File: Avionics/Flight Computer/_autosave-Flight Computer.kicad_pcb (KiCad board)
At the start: 2 copper layers, 50.8 x 50.8 mm, 28 parts, among them J1 CONN_COAXIAL, J2 CONN_COAXIAL, U1 CC1310F128RGZR, U2 CC1190RGVR, U3 CC2650F128RGZR, U4 CC2592RGVR

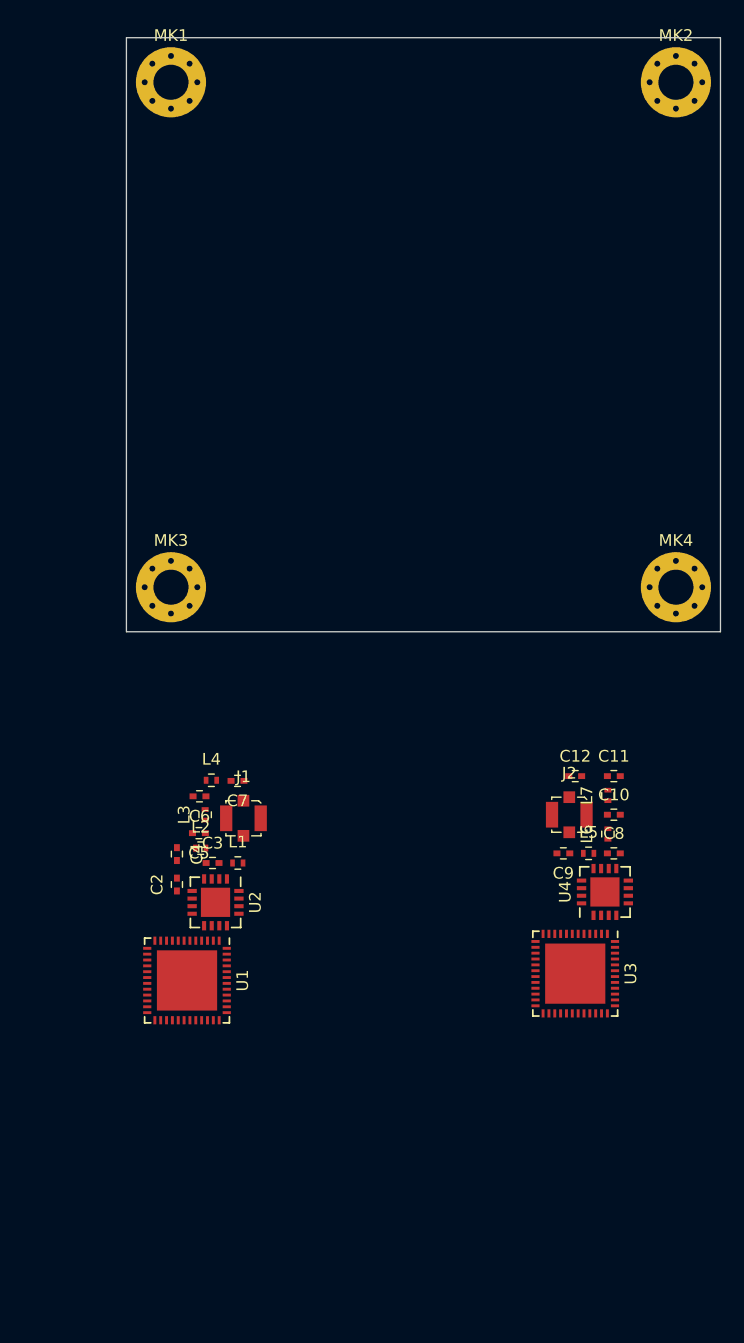
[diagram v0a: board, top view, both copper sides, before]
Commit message: Added framework and started capturing radio schematics.
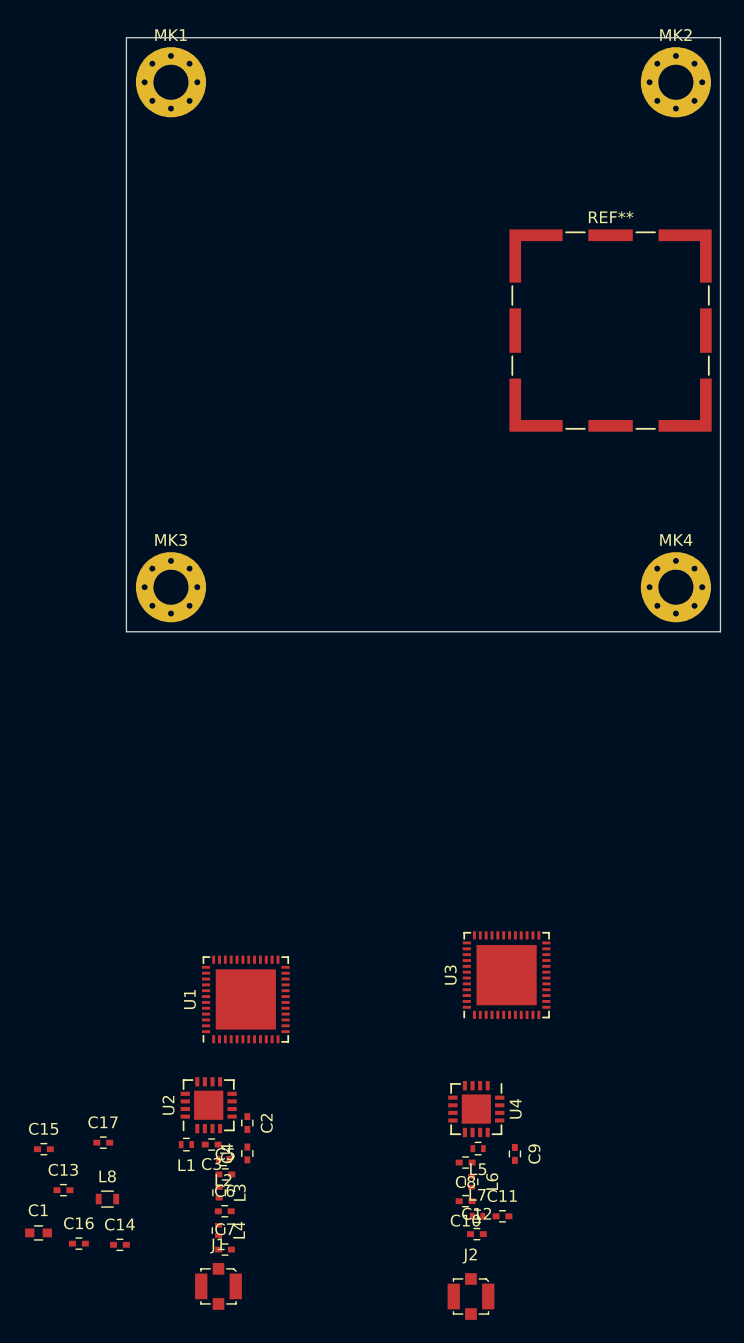
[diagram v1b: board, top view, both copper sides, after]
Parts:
- added C1: C, Capacitors_SMD:C_0603, F.Cu at (48.7, 170.0)
- added C13: C, Capacitors_SMD:C_0402, F.Cu at (50.8, 166.4)
- added C14: C, Capacitors_SMD:C_0402, F.Cu at (55.6, 171.0)
- added C15: C, Capacitors_SMD:C_0402, F.Cu at (49.1, 162.9)
- added C16: C, Capacitors_SMD:C_0402, F.Cu at (52.1, 170.9)
- added C17: C, Capacitors_SMD:C_0402, F.Cu at (54.2, 162.3)
- added L8: L, Inductors_SMD:L_0603, F.Cu at (54.6, 167.1)
- added REF**: Laird_Technologies_BMI-S-202-F_16.50x16.50mm, Shielding_Cabinets:Laird_Technologies_BMI-S-202-F_16.50x16.50mm, F.Cu at (97.6, 92.9)
- moved J2 42.0 mm to (85.7, 175.5)
- moved C7 40.1 mm to (64.6, 171.4), turned to 0 degrees
- moved J1 40.1 mm to (64.1, 174.6)
- moved C12 40.1 mm to (86.2, 170.1)
- moved C11 38.8 mm to (88.3, 168.6)
- moved L4 38.5 mm to (64.1, 169.8), turned to 270 degrees
- moved L7 37.7 mm to (86.2, 168.6), turned to 0 degrees
- moved C6 35.5 mm to (64.6, 168.2), turned to 0 degrees
- moved C10 35.4 mm to (85.2, 167.3), turned to 180 degrees
- moved L3 32.4 mm to (64.1, 166.6), turned to 270 degrees
- moved L6 31.9 mm to (85.7, 165.6), turned to 270 degrees
- moved C8 29.3 mm to (85.2, 164.0), turned to 180 degrees
- moved C5 29.3 mm to (64.6, 165.0), turned to 0 degrees
- moved L5 27.0 mm to (86.3, 162.8), turned to 180 degrees
- moved L2 26.7 mm to (64.5, 163.7), turned to 180 degrees
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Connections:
- U1 pad 1: Net-(U1-Pad1) -> Net-(C14-Pad2)
- U2 pad 10: Net-(U1-Pad1) -> Net-(C14-Pad1)
- U2 pad 11: Net-(U1-Pad1) -> Net-(C14-Pad1)
- U2 pad 13: Net-(U2-Pad13) -> Net-(L1-Pad2)
- U2 pad 15: Net-(U2-Pad15) -> Net-(L1-Pad2)
- U2 pad 16: Net-(U2-Pad16) -> Net-(L1-Pad2)
